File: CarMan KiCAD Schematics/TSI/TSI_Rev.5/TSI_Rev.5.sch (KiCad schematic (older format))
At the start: 36 parts, among them J1 TSV, J10 Breakered GLV, J11 Dashboard/EPAL, J12 Battery Packs SL, J13 RSP Safety Loop, J14.1 Logic Conn. 1, J14.2 Logic Conn. 2, J15 Roll Hoop TSAL, J16 Throttle Plau., J17 Brakes & BOT SL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

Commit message: Small aesthetic changes
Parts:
- J10: value Breakered GLV -> J10 GLV PWR
- J11: value Dashboard/EPAL -> J11 DASH/EPAL
- J12: value Battery Packs SL -> J12 BP SL
- J13: value RSP Safety Loop -> J13 RSP SL
- J15: value Roll Hoop TSAL -> J15 ROLL TSAL
- J16: value Throttle Plau. -> J16 THROTTLE PLAUS.
- J17: value Brakes & BOT SL -> J17 BRAKES
- J18: value RTDS & Brk Light -> J18 RTDS & BRK LIGHT
- J19: value Cooling Sensors -> J19 COOL SENSORS
- J20: value IMD & AMS BTN -> J20 LSP
- J21: value I2C -> J21 I2C
- J6: value IMD -> J6 IMD
- J7: value BP Can & Power -> J7 BP CAN & PWR
- J8: value Cockpit -> J8 COCKPIT
- J9: value Cooling Power -> J9 COOL PWR
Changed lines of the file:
@@
 P 4800 1600
 F 0 "J13" H 4750 1800 50  0000 L CNN
-F 1 "RSP Safety Loop" H 4750 1800 50  0001 L CNN
+F 1 "J13 RSP SL" H 4750 1800 50  0001 L CNN
 F 2 "TSI_Rev_2021_Footprint_Lib:Molex_MiniFit-JR-5556-04A_2x02x4.20mm_Straight" H 4800 1600 50  0001 C CNN
 F 3 "~" H 4800 1600 50  0001 C CNN
@@
 Text Notes 3975 925  0    50   ~ 0
 Discharge Relay (NC)
-$Comp
-L Connector_Generic:Conn_02x04_Counter_Clockwise J6
-U 1 1 60243E54
-P 5700 775
-F 0 "J6" H 5750 975 50  0000 C CNN
-F 1 "IMD" H 5750 975 50  0001 C CNN
-F 2 "TSI_Rev_2021_Footprint_Lib:Molex_MiniFit-JR-5556-08A_2x04x4.20mm_Straight" H 5700 775 50  0001 C CNN
-F 3 "~" H 5700 775 50  0001 C CNN
-	1    5700 775
-	1    0    0    -1
-$EndComp
 NoConn ~ 6000 775
 NoConn ~ 6000 875
@@
 P 1500 2675
 F 0 "J19" H 1450 2975 50  0000 L CNN
-F 1 "Cooling Sensors" H 1450 2975 50  0001 L CNN
+F 1 "J19 COOL SENSORS" H 1450 2975 50  0001 L CNN
 F 2 "TSI_Rev_2021_Footprint_Lib:Molex_MiniFit-JR-5556-06A_2x03x4.20mm_Straight" H 1500 2675 50  0001 C CNN
 F 3 "~" H 1500 2675 50  0001 C CNN
@@
 P 8950 775
 F 0 "J8" H 8900 975 50  0000 L CNN
-F 1 "Cockpit" H 8900 975 50  0001 L CNN
+F 1 "J8 COCKPIT" H 8900 975 50  0001 L CNN
 F 2 "TSI_Rev_2021_Footprint_Lib:Molex_MiniFit-JR-5556-04A_2x02x4.20mm_Straight" H 8950 775 50  0001 C CNN
 F 3 "~" H 8950 775 50  0001 C CNN
@@
 P 7950 875
 F 0 "J7" H 7900 1175 50  0000 L CNN
-F 1 "BP Can & Power" H 8030 776 50  0001 L CNN
+F 1 "J7 BP CAN & PWR" H 8030 776 50  0001 L CNN
 F 2 "TSI_Rev_2021_Footprint_Lib:Molex_MiniFit-JR-5556-06A_2x03x4.20mm_Straight" H 7950 875 50  0001 C CNN
 F 3 "~" H 7950 875 50  0001 C CNN
@@
 P 3825 1600
 F 0 "J12" H 3775 1800 50  0000 L CNN
-F 1 "Battery Packs SL" H 3775 1800 50  0001 L CNN
+F 1 "J12 BP SL" H 3775 1800 50  0001 L CNN
 F 2 "TSI_Rev_2021_Footprint_Lib:Molex_MiniFit-JR-5556-04A_2x02x4.20mm_Straight" H 3825 1600 50  0001 C CNN
 F 3 "~" H 3825 1600 50  0001 C CNN
@@
 P 2675 2600
 F 0 "J20" H 2625 2800 50  0000 L CNN
-F 1 "IMD & AMS BTN" H 2625 2800 50  0001 L CNN
+F 1 "J20 LSP" H 2625 2800 50  0001 L CNN
 F 2 "TSI_Rev_2021_Footprint_Lib:Molex_MiniFit-JR-5556-04A_2x02x4.20mm_Straight" H 2675 2600 50  0001 C CNN
 F 3 "~" H 2675 2600 50  0001 C CNN
@@
 P 10850 775
 F 0 "J10" H 10800 975 50  0000 L CNN
-F 1 "Breakered GLV" H 10800 975 50  0001 L CNN
+F 1 "J10 GLV PWR" H 10800 975 50  0001 L CNN
 F 2 "TSI_Rev_2021_Footprint_Lib:Molex_MiniFit-JR-5556-04A_2x02x4.20mm_Straight" H 10850 775 50  0001 C CNN
 F 3 "~" H 10850 775 50  0001 C CNN
@@
 P 2975 1800
 F 0 "J11" H 2925 2200 50  0000 L CNN
-F 1 "Dashboard/EPAL" H 3055 1701 50  0001 L CNN
+F 1 "J11 DASH/EPAL" H 3055 1701 50  0001 L CNN
 F 2 "TSI_Rev_2021_Footprint_Lib:Molex_MiniFit-JR-5556-08A_2x04x4.20mm_Straight" H 2975 1800 50  0001 C CNN
 F 3 "~" H 2975 1800 50  0001 C CNN
@@
 P 9975 1600
 F 0 "J17" H 9925 1800 50  0000 L CNN
-F 1 "Brakes & BOT SL" H 9925 1800 50  0001 L CNN
+F 1 "J17 BRAKES" H 9925 1800 50  0001 L CNN
 F 2 "TSI_Rev_2021_Footprint_Lib:Molex_MiniFit-JR-5556-04A_2x02x4.20mm_Straight" H 9975 1600 50  0001 C CNN
 F 3 "~" H 9975 1600 50  0001 C CNN
@@
 P 8875 1700
 F 0 "J16" H 8825 2000 50  0000 L CNN
-F 1 "Throttle Plau." H 8825 2000 50  0001 L CNN
+F 1 "J16 THROTTLE PLAUS." H 8825 2000 50  0001 L CNN
 F 2 "TSI_Rev_2021_Footprint_Lib:Molex_MiniFit-JR-5556-06A_2x03x4.20mm_Straight" H 8875 1700 50  0001 C CNN
 F 3 "~" H 8875 1700 50  0001 C CNN
@@
 P 8025 1500
 F 0 "J15" H 7975 1600 50  0000 L CNN
-F 1 "Roll Hoop TSAL" H 7975 1600 50  0001 L CNN
+F 1 "J15 ROLL TSAL" H 7975 1600 50  0001 L CNN
 F 2 "TSI_Rev_2021_Footprint_Lib:Molex_MiniFit-JR-5556-02A_2x01x4.20mm_Straight" H 8025 1500 50  0001 C CNN
 F 3 "~" H 8025 1500 50  0001 C CNN
@@
 P 11000 1600
 F 0 "J18" H 10950 1800 50  0000 L CNN
-F 1 "RTDS & Brk Light" H 10950 1800 50  0001 L CNN
+F 1 "J18 RTDS & BRK LIGHT" H 10950 1800 50  0001 L CNN
 F 2 "TSI_Rev_2021_Footprint_Lib:Molex_MiniFit-JR-5556-04A_2x02x4.20mm_Straight" H 11000 1600 50  0001 C CNN
 F 3 "~" H 11000 1600 50  0001 C CNN
@@
 P 3550 2600
 F 0 "J21" H 3475 2800 50  0000 L CNN
-F 1 "I2C" H 3500 2700 50  0001 L CNN
+F 1 "J21 I2C" H 3500 2700 50  0001 L CNN
 F 2 "Connector_PinSocket_2.54mm:PinSocket_1x04_P2.54mm_Vertical" H 3550 2600 50  0001 C CNN
 F 3 "~" H 3550 2600 50  0001 C CNN
@@
 P 9800 675
 F 0 "J9" H 9750 775 50  0000 L CNN
-F 1 "Cooling Power" H 9750 775 50  0001 L CNN
+F 1 "J9 COOL PWR" H 9750 775 50  0001 L CNN
 F 2 "TSI_Rev_2021_Footprint_Lib:Molex_MiniFit-JR-5556-02A_2x01x4.20mm_Straight" H 9800 675 50  0001 C CNN
 F 3 "~" H 9800 675 50  0001 C CNN
@@
 Text Label 8100 3850 0    49   ~ 0
 5V
+$Comp
+L Connector_Generic:Conn_02x04_Counter_Clockwise J6
+U 1 1 60243E54
+P 5700 775
+F 0 "J6" H 5750 975 50  0000 C CNN
+F 1 "J6 IMD" H 5750 975 50  0001 C CNN
+F 2 "TSI_Rev_2021_Footprint_Lib:Molex_MiniFit-JR-5556-08A_2x04x4.20mm_Straight" H 5700 775 50  0001 C CNN
+F 3 "~" H 5700 775 50  0001 C CNN
+	1    5700 775
+	1    0    0    -1
+$EndComp
 $EndSCHEMATC

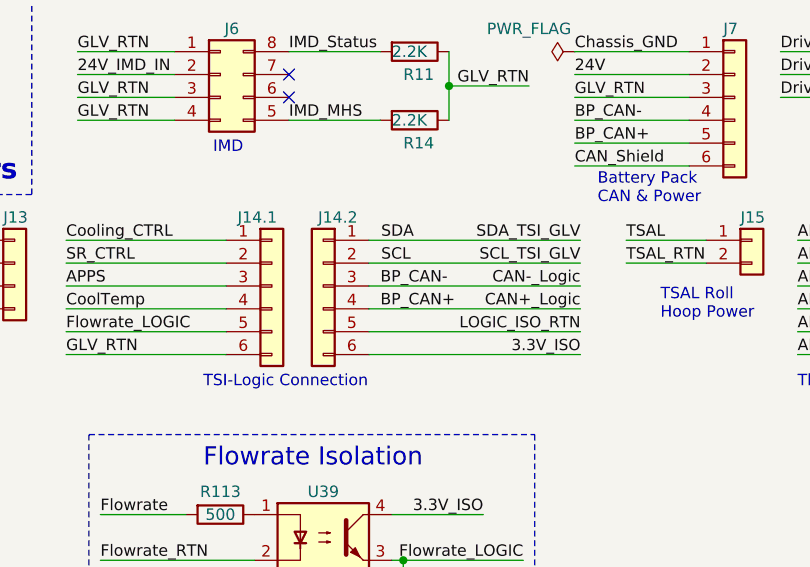
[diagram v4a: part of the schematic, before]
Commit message: More TSI routing optimization
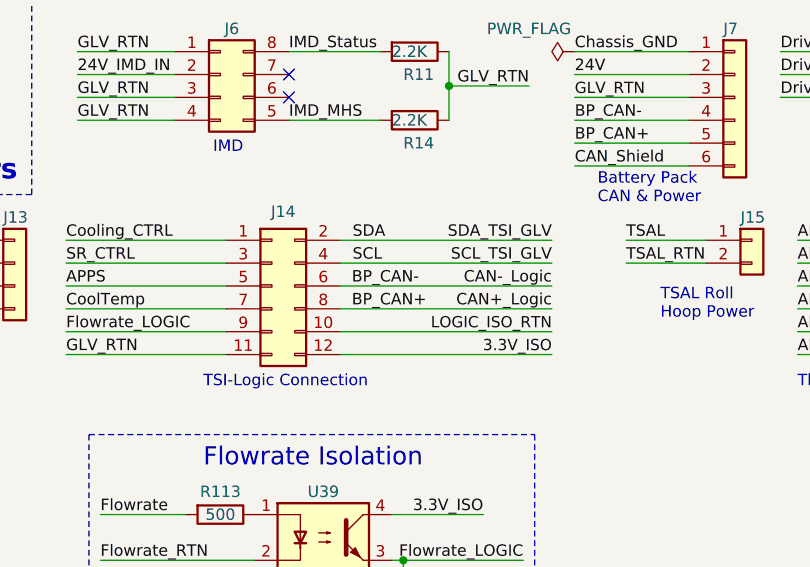
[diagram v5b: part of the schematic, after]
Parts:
- removed J14.1: Logic Conn. 1, Connector_PinSocket_2.54mm:PinSocket_1x06_P2.54mm_Vertical, symbol Connector_Generic:Conn_01x06
- removed J14.2: Logic Conn. 2, Connector_PinSocket_2.54mm:PinSocket_1x06_P2.54mm_Vertical, symbol Connector_Generic:Conn_01x06
- added J14: Conn_02x06_Odd_Even, Connector_PinSocket_2.54mm:PinSocket_2x06_P2.54mm_Vertical, symbol Connector_Generic:Conn_02x06_Odd_Even
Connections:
- net 3.3V_ISO: now also J14.12 (Pin_12)
- net AIRS-: now also J14.11 (Pin_11)
- net APPS: now also J14.5 (Pin_5)
- net BP_CAN+: now also J14.8 (Pin_8)
- net BP_CAN-: now also J14.6 (Pin_6)
- net CoolTemp: now also J14.7 (Pin_7)
- net Cooling_CTRL: now also J14.1 (Pin_1)
- net Flowrate_LOGIC: now also J14.9 (Pin_9)
- net LOGIC_ISO_RTN: now also J14.10 (Pin_10)
- net SCL: now also J14.4 (Pin_4)
- net SDA: now also J14.2 (Pin_2)
- net SR_CTRL: now also J14.3 (Pin_3)
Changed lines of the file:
@@
 Text Label 8100 5325 0    50   ~ 0
 AIRS-
-Text Label 7275 1600 2    50   ~ 0
+Text Label 7150 1600 2    50   ~ 0
 SCL_TSI_GLV
-Text Label 7275 1500 2    50   ~ 0
+Text Label 7150 1500 2    50   ~ 0
 SDA_TSI_GLV
 Text Label 5025 1500 0    50   ~ 0
@@
 Text Label 11100 3150 2    50   ~ 0
 RTDS
-$Comp
-L Connector_Generic:Conn_01x06 J14.2
-U 1 1 5FC777B8
-P 6150 1700
-F 0 "J14.2" H 6000 2000 50  0000 L CNN
-F 1 "Logic Conn. 2" H 6230 1601 50  0001 L CNN
-F 2 "Connector_PinSocket_2.54mm:PinSocket_1x06_P2.54mm_Vertical" H 6150 1700 50  0001 C CNN
-F 3 "~" H 6150 1700 50  0001 C CNN
-	1    6150 1700
-	-1   0    0    -1
-$EndComp
-$Comp
-L Connector_Generic:Conn_01x06 J14.1
-U 1 1 5FC77F26
-P 5925 1700
-F 0 "J14.1" H 5775 2000 50  0000 L CNN
-F 1 "Logic Conn. 1" H 6005 1601 50  0001 L CNN
-F 2 "Connector_PinSocket_2.54mm:PinSocket_1x06_P2.54mm_Vertical" H 5925 1700 50  0001 C CNN
-F 3 "~" H 5925 1700 50  0001 C CNN
-	1    5925 1700
-	1    0    0    -1
-$EndComp
 Wire Wire Line
 	525  775  725  775
@@
 Wire Wire Line
 	8100 3750 8850 3750
-Text Label 7275 1900 2    49   ~ 0
+Text Label 7150 1900 2    49   ~ 0
 LOGIC_ISO_RTN
 Text Label 8100 3750 0    49   ~ 0
@@
 Wire Notes Line
 	4875 475  4875 1300
-Text Label 6400 1700 0    50   ~ 0
+Text Label 6275 1700 0    50   ~ 0
 BP_CAN-
-Text Label 6400 1800 0    50   ~ 0
+Text Label 6275 1800 0    50   ~ 0
 BP_CAN+
 Text Notes 2225 1150 0    43   ~ 0
@@
     (2A > to open, \n 90mA nominal draw)
 Wire Wire Line
-	6350 1800 7275 1800
-Wire Wire Line
-	7275 1700 6350 1700
+	6225 1800 7150 1800
+Wire Wire Line
+	7150 1700 6225 1700
 Text Label 700  5450 0    50   ~ 0
 RTDS_CTRL
-Text Label 7275 1800 2    50   ~ 0
+Text Label 7150 1800 2    50   ~ 0
 CAN+_Logic
-Text Label 7275 1700 2    50   ~ 0
+Text Label 7150 1700 2    50   ~ 0
 CAN-_Logic
 Text Label 5025 1600 0    50   ~ 0
@@
 APPS
 Wire Wire Line
-	6350 1900 7275 1900
-Text Label 6403 1600 0    50   ~ 0
+	6225 1900 7150 1900
+Text Label 6278 1600 0    50   ~ 0
 SCL
-Text Label 6403 1500 0    50   ~ 0
+Text Label 6278 1500 0    50   ~ 0
 SDA
 Wire Notes Line
@@
 	5150 3465 7070 3465
 Wire Wire Line
-	6350 1600 7275 1600
-Wire Wire Line
-	6350 1500 7275 1500
-Text Label 7275 2000 2    49   ~ 0
+	6225 1600 7150 1600
+Wire Wire Line
+	6225 1500 7150 1500
+Text Label 7150 2000 2    49   ~ 0
 3.3V_ISO
 Wire Wire Line
-	6350 2000 7275 2000
+	6225 2000 7150 2000
 $Comp
 L Device:R R?
@@
 	1    0    0    -1
 $EndComp
+$Comp
+L Connector_Generic:Conn_02x06_Odd_Even J14
+U 1 1 608971D0
+P 5925 1700
+F 0 "J14" H 5975 2025 50  0000 C CNN
+F 1 "Conn_02x06_Odd_Even" H 5975 2026 50  0001 C CNN
+F 2 "Connector_PinSocket_2.54mm:PinSocket_2x06_P2.54mm_Vertical" H 5925 1700 50  0001 C CNN
+F 3 "~" H 5925 1700 50  0001 C CNN
+	1    5925 1700
+	1    0    0    -1
+$EndComp

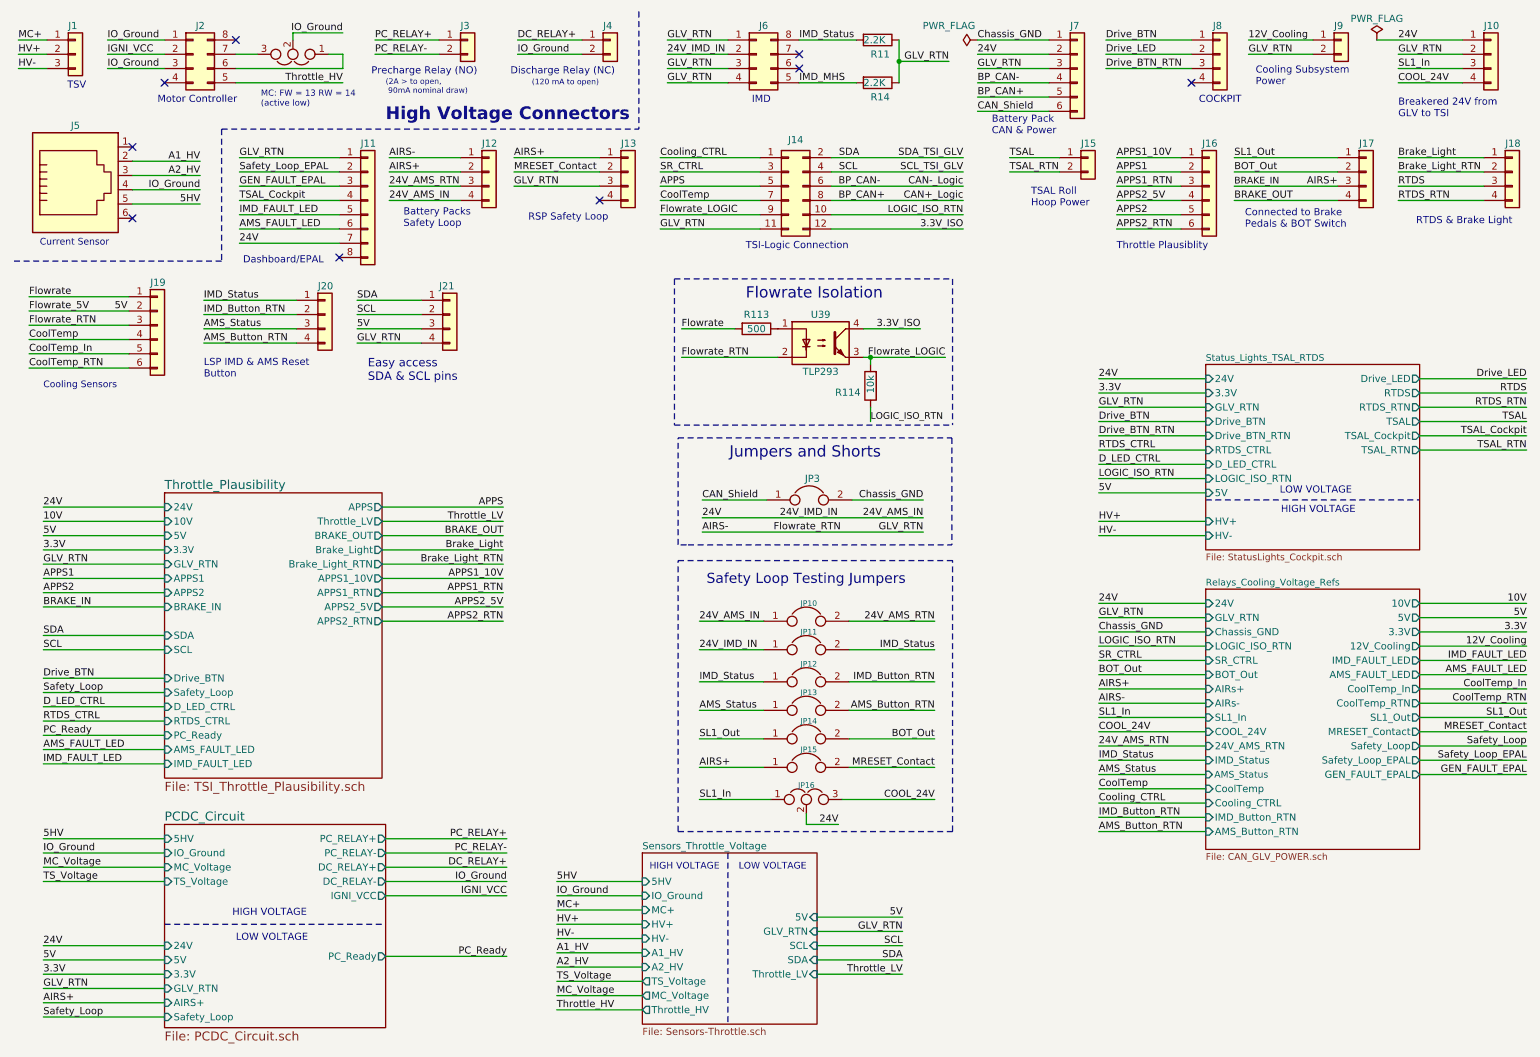
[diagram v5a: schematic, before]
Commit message: TSI Logic changes the 2nd
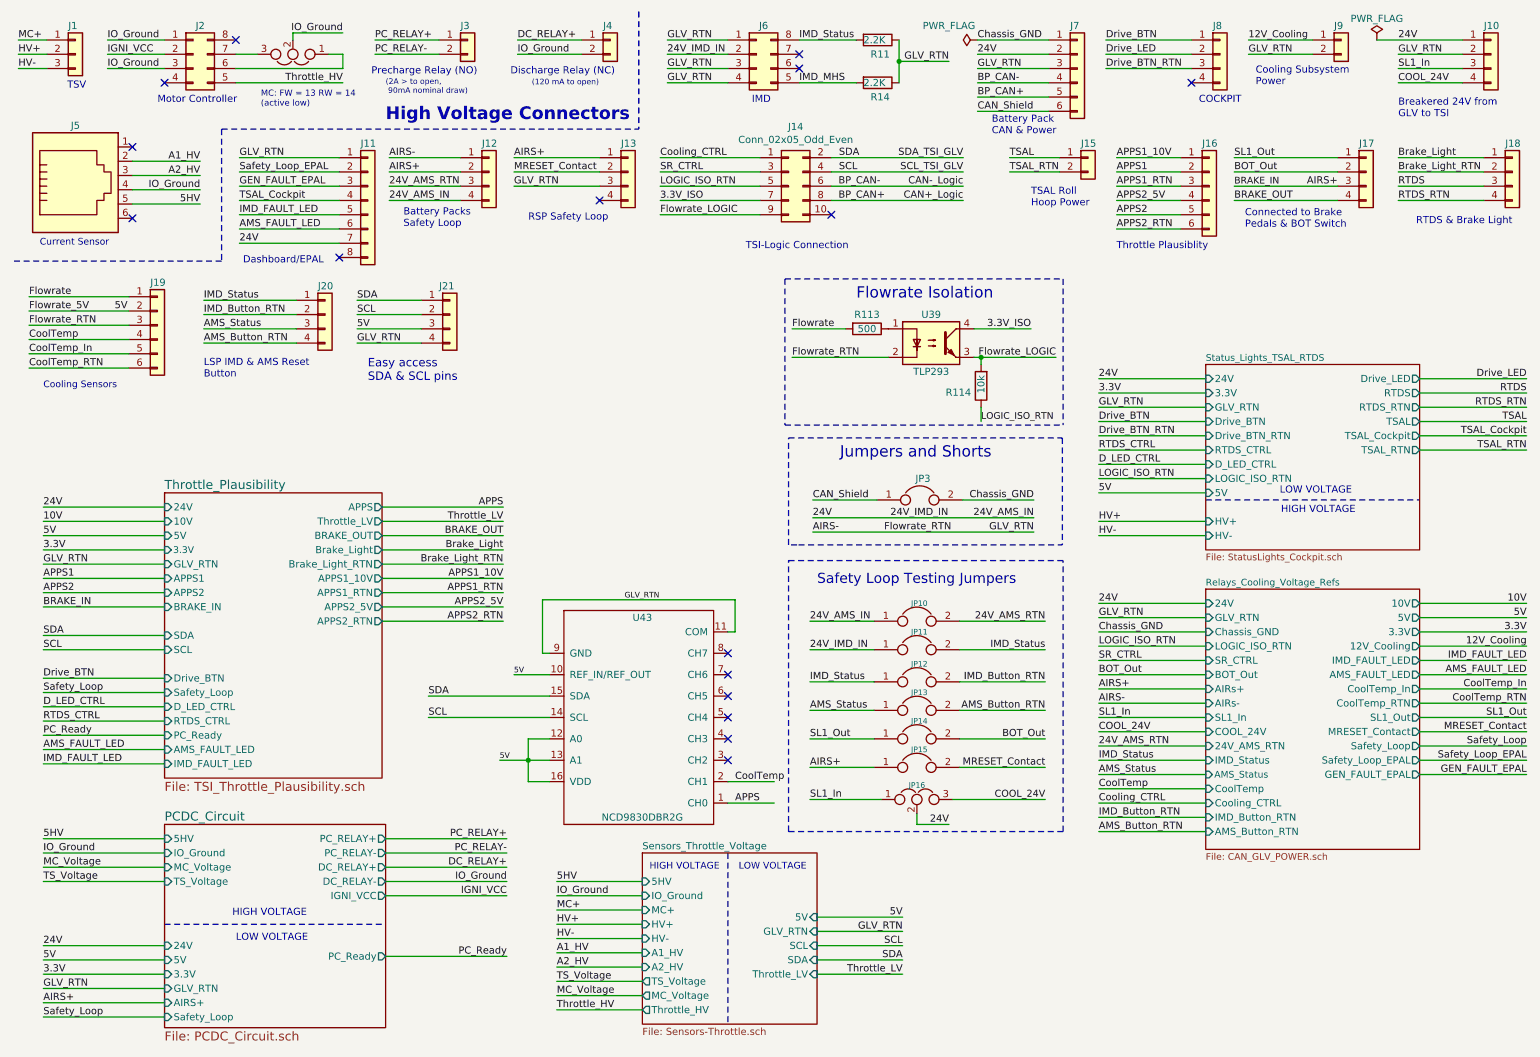
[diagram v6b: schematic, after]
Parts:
- removed J14: Conn_02x06_Odd_Even, Connector_PinSocket_2.54mm:PinSocket_2x06_P2.54mm_Vertical, symbol Connector_Generic:Conn_02x06_Odd_Even
- added J14: Conn_02x05_Odd_Even, Connector_PinSocket_2.54mm:PinSocket_2x05_P2.54mm_Vertical, symbol Connector_Generic:Conn_02x05_Odd_Even
- added U43: NCD9830DBR2G, TSI_Rev_2021_Footprint_Lib:SOP65P640X120-16N, symbol TSI_Rev.5-rescue:NCD9830DBR2G-CarMan_KiCAD_Library-TSI_Rev.5-rescue
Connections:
- net 3.3V_ISO: now also J14.7 (Pin_7)
- net 5V: now also U43.10 (REF_IN/REF_OUT), U43.12 (A0), U43.13 (A1), U43.16 (VDD)
- net AIRS-: now also U43.11 (COM), U43.9 (GND)
- net APPS: now also U43.1 (CH0)
- net BP_CAN+: now also J14.8 (Pin_8)
- net BP_CAN-: now also J14.6 (Pin_6)
- net CoolTemp: now also U43.2 (CH1)
- net Cooling_CTRL: now also J14.1 (Pin_1)
- net Flowrate_LOGIC: now also J14.9 (Pin_9)
- net LOGIC_ISO_RTN: now also J14.5 (Pin_5)
- net SCL: now also J14.4 (Pin_4), U43.14 (SCL)
- net SDA: now also J14.2 (Pin_2), U43.15 (SDA)
- net SR_CTRL: now also J14.3 (Pin_3)
- no-connect marks 9 -> 16
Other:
- moved on the sheet: JP10, JP11, JP12, JP13, JP14, JP15, JP16, JP3, R113, R114, U39

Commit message: Updated board
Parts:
- removed R113: 500, Resistor_SMD:R_0805_2012Metric_Pad1.15x1.40mm_HandSolder, symbol Device:R
- removed R114: 10k, Resistor_SMD:R_0805_2012Metric_Pad1.15x1.40mm_HandSolder, symbol Device:R
- removed U39: TLP293, Package_SO:SOIC-4_4.55x2.6mm_P1.27mm, symbol TSI_Rev.5-rescue:TLP293-CarMan_KiCAD_Library-TSI_Rev.5-rescue
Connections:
- net AIRS-: no longer J19.3 (Pin_3)
- new net Flowrate_RTN: J19.3 (Pin_3)
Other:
- note removed: "Flowrate Isolation"
- moved on the sheet: JP10, JP11, JP12, JP13, JP14, JP15, JP16, JP3

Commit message: Updated TSI Schematic
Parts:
- removed U43: NCD9830DBR2G, TSI_Rev_2021_Footprint_Lib:SOP65P640X120-16N, symbol TSI_Rev.5-rescue:NCD9830DBR2G-CarMan_KiCAD_Library-TSI_Rev.5-rescue
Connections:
- no-connect marks 16 -> 10
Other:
- moved on the sheet: JP10, JP11, JP12, JP13, JP14, JP15, JP16, JP3
